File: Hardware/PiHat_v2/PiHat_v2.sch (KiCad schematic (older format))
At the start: 31 parts, among them P1 CONN_02X20, P2 CONN_01X02, P3 CONN_01X08

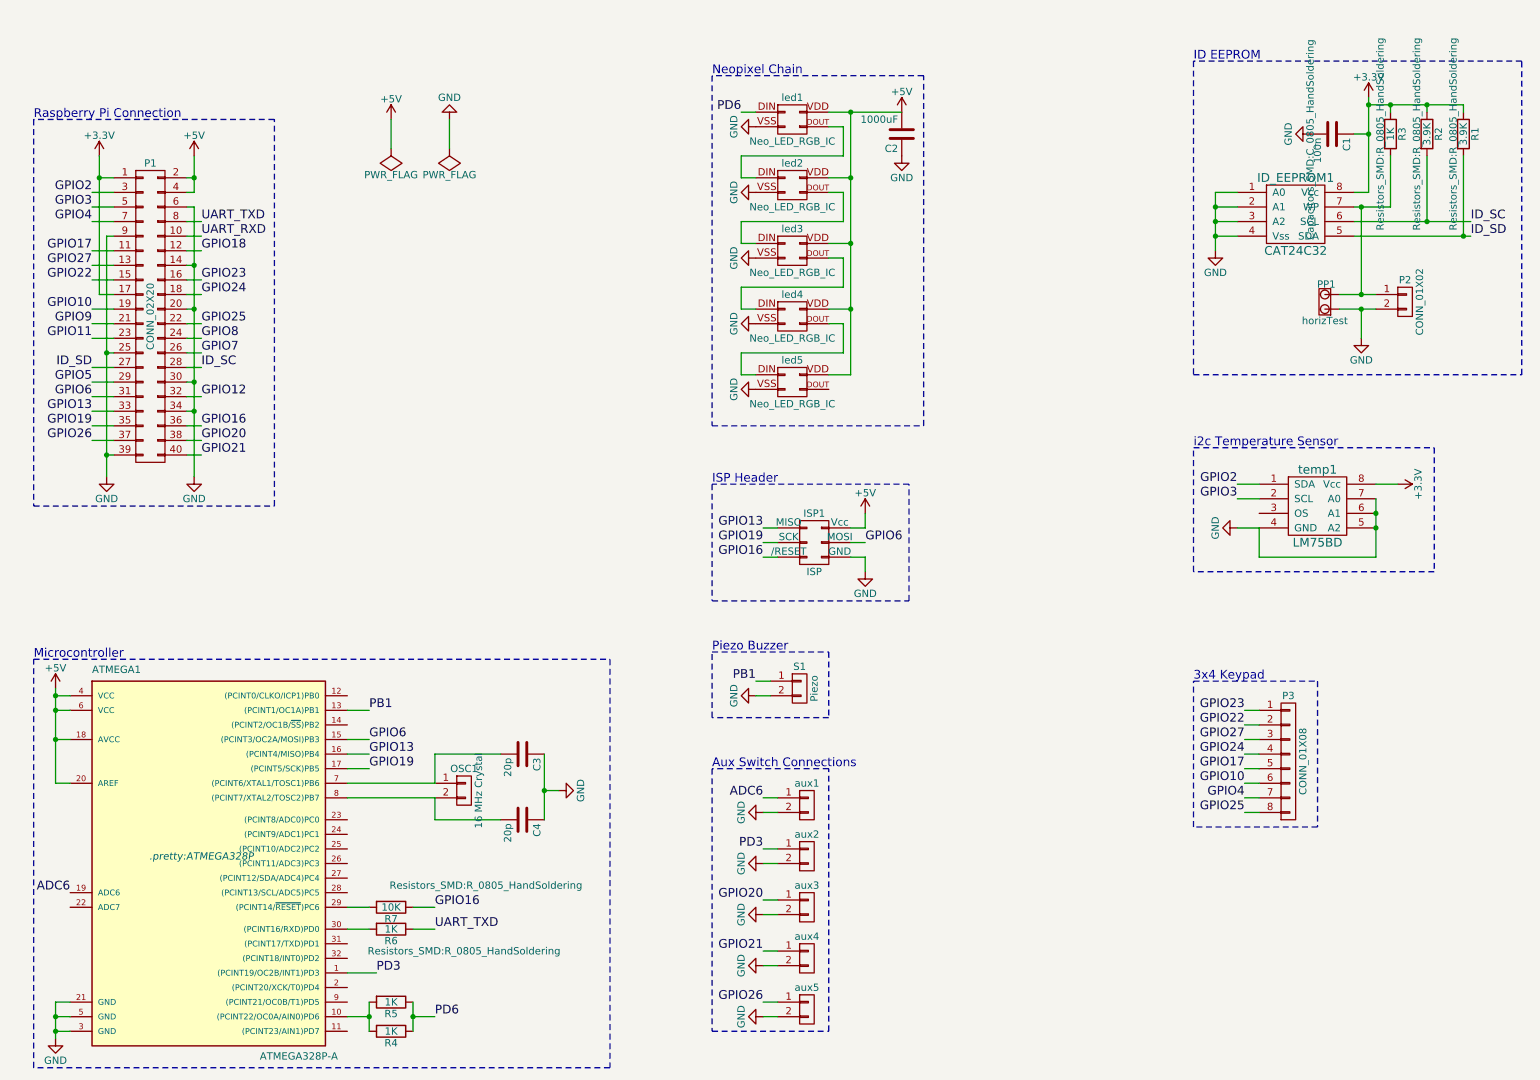
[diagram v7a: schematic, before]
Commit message: Update Aux Connector Pin Directions
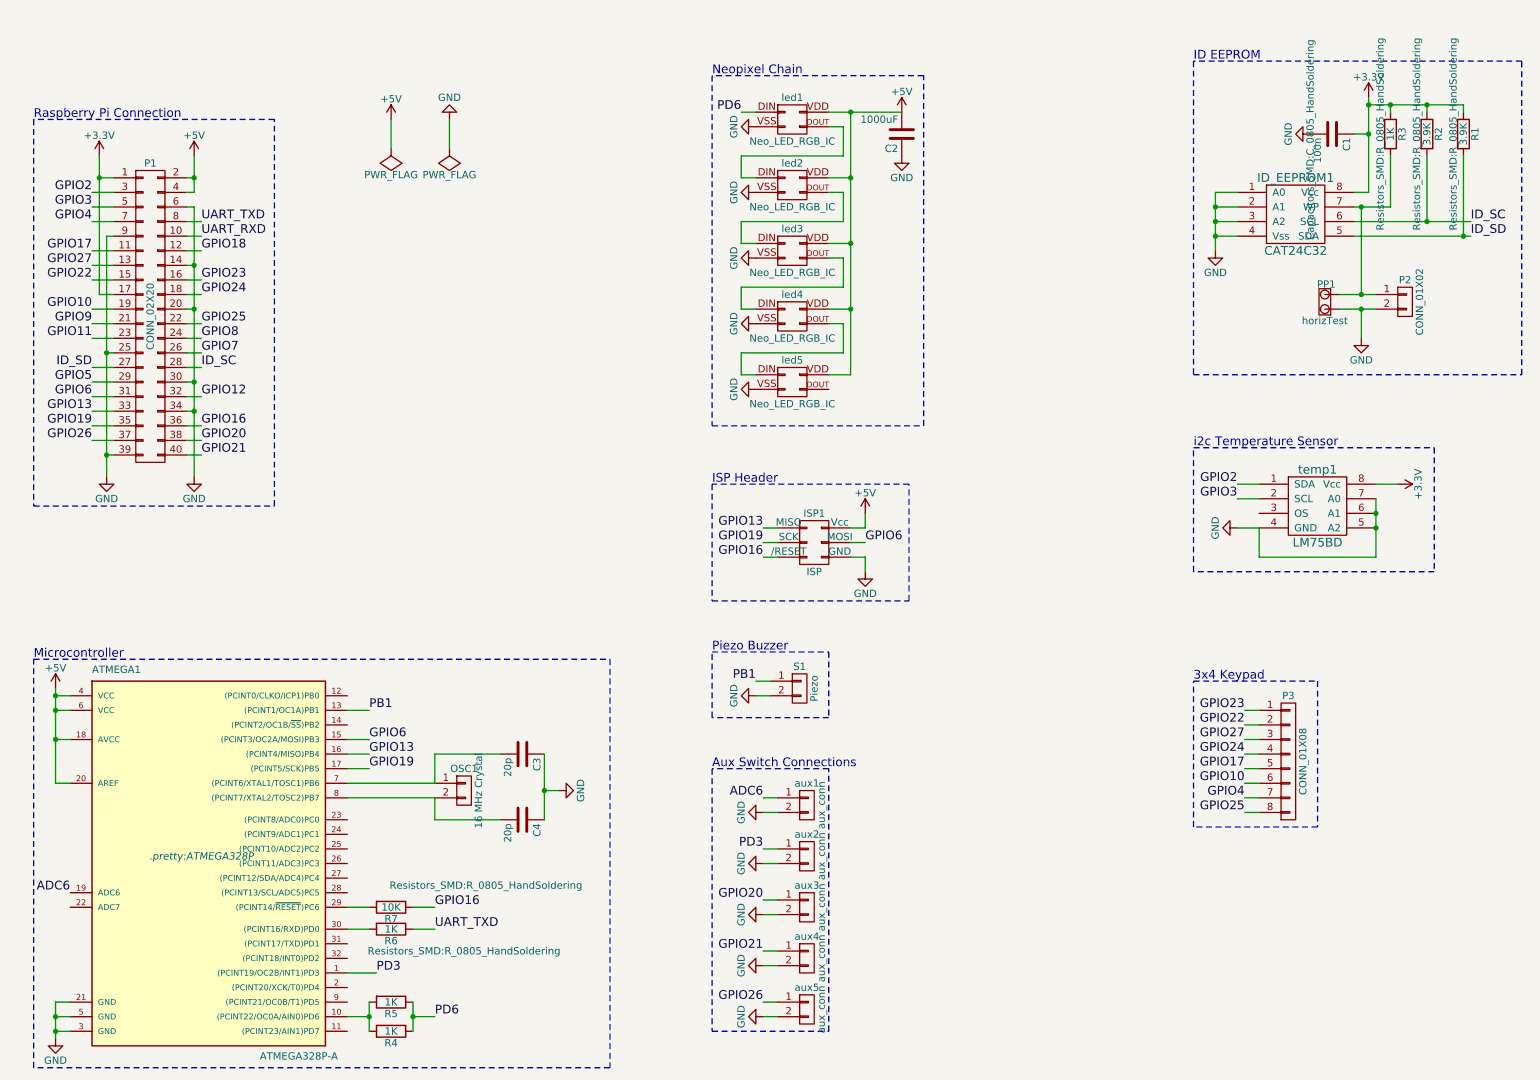
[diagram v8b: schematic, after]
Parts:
- removed aux1, aux2, aux3, aux4, aux5: CONN_01X02, Connectors_Molex:Molex_KK-6410-02_02x2.54mm_Straight, symbol CONN_01X02
- added aux1, aux2, aux3, aux4, aux5: aux_conn, symbol aux_conn
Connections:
- net ADC6: now also aux1.1 (P1)
- net GND: now also aux1.2 (P2), aux2.2 (P2), aux3.2 (P2), aux4.2 (P2), aux5.2 (P2)
- net GPIO20: now also aux3.1 (P1)
- net GPIO21: now also aux4.1 (P1)
- net GPIO26: now also aux5.1 (P1)
- net PD3: now also aux2.1 (P1)
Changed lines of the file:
@@
-$EndComp
-$Comp
-L CONN_01X02 aux1
-U 1 1 5888D1B3
-P 6050 5850
-F 0 "aux1" H 6050 6000 50  0000 C CNN
-F 1 "CONN_01X02" V 6150 5850 50  0001 C CNN
-F 2 "Connectors_Molex:Molex_KK-6410-02_02x2.54mm_Straight" H 6050 5850 50  0001 C CNN
-F 3 "" H 6050 5850 50  0000 C CNN
-	1    6050 5850
-	1    0    0    -1
 $EndComp
 $Comp
@@
 $EndComp
 $Comp
-L CONN_01X02 aux3
-U 1 1 588926FD
-P 6050 6550
-F 0 "aux3" H 6050 6700 50  0000 C CNN
-F 1 "CONN_01X02" V 6150 6550 50  0001 C CNN
-F 2 "Connectors_Molex:Molex_KK-6410-02_02x2.54mm_Straight" H 6050 6550 50  0001 C CNN
-F 3 "" H 6050 6550 50  0000 C CNN
-	1    6050 6550
-	1    0    0    -1
-$EndComp
-$Comp
 L GND #PWR011
 U 1 1 58893B93
@@
 $EndComp
 $Comp
-L CONN_01X02 aux2
-U 1 1 58893B9A
-P 6050 6200
-F 0 "aux2" H 6050 6350 50  0000 C CNN
-F 1 "CONN_01X02" V 6150 6200 50  0001 C CNN
-F 2 "Connectors_Molex:Molex_KK-6410-02_02x2.54mm_Straight" H 6050 6200 50  0001 C CNN
-F 3 "" H 6050 6200 50  0000 C CNN
-	1    6050 6200
-	1    0    0    -1
-$EndComp
-$Comp
 L GND #PWR012
 U 1 1 58893BEF
@@
 	1    5750 6950
 	0    1    1    0
-$EndComp
-$Comp
-L CONN_01X02 aux4
-U 1 1 58893BF6
-P 6050 6900
-F 0 "aux4" H 6050 7050 50  0000 C CNN
-F 1 "CONN_01X02" V 6150 6900 50  0001 C CNN
-F 2 "Connectors_Molex:Molex_KK-6410-02_02x2.54mm_Straight" H 6050 6900 50  0001 C CNN
-F 3 "" H 6050 6900 50  0000 C CNN
-	1    6050 6900
-	1    0    0    -1
 $EndComp
 $Comp
@@
 F 3 "" H 5950 -50 50  0000 C CNN
 	1    5950 1150
-	1    0    0    -1
-$EndComp
-$Comp
-L CONN_01X02 aux5
-U 1 1 58941875
-P 6050 7250
-F 0 "aux5" H 6050 7400 50  0000 C CNN
-F 1 "CONN_01X02" V 6150 7250 50  0001 C CNN
-F 2 "Connectors_Molex:Molex_KK-6410-02_02x2.54mm_Straight" H 6050 7250 50  0001 C CNN
-F 3 "" H 6050 7250 50  0000 C CNN
-	1    6050 7250
 	1    0    0    -1
 $EndComp
@@
 Connection ~ 900  5200
 Wire Wire Line
-	1000 5200 900  5200
+	900  5200 1000 5200
 Wire Notes Line
 	750  4850 4700 4850
@@
 Connection ~ 900  7400
 Wire Wire Line
-	1000 7400 900  7400
+	900  7400 1000 7400
 Wire Wire Line
 	900  7200 900  7450
@@
 Connection ~ 9950 3850
 Wire Wire Line
-	9950 4150 9950 3750
+	9950 3750 9950 4150
 Wire Notes Line
 	8700 4250 8700 3400
@@
 Connection ~ 9950 3950
 Wire Wire Line
-	9150 4150 9950 4150
-Wire Wire Line
-	9150 3950 9150 4150
+	9950 4150 9150 4150
+Wire Wire Line
+	9150 4150 9150 3950
 Wire Wire Line
 	9150 5900 9050 5900
@@
 	9950 3650 10100 3650
 Wire Wire Line
-	9000 3950 9150 3950
+	9150 3950 9000 3950
 Wire Wire Line
 	9000 3650 9150 3650
@@
 Wire Wire Line
 	3600 1150 3600 1350
+$Comp
+L aux_conn aux1
+U 1 1 5946D2A9
+P 6050 5850
+F 0 "aux1" H 6050 6000 50  0000 C CNN
+F 1 "aux_conn" V 6150 5850 50  0000 C CNN
+F 2 "" H 6050 5850 50  0000 C CNN
+F 3 "" H 6050 5850 50  0000 C CNN
+	1    6050 5850
+	1    0    0    -1
+$EndComp
+$Comp
+L aux_conn aux2
+U 1 1 5946D408
+P 6050 6200
+F 0 "aux2" H 6050 6350 50  0000 C CNN
+F 1 "aux_conn" V 6150 6200 50  0000 C CNN
+F 2 "" H 6050 6200 50  0000 C CNN
+F 3 "" H 6050 6200 50  0000 C CNN
+	1    6050 6200
+	1    0    0    -1
+$EndComp
+$Comp
+L aux_conn aux3
+U 1 1 5946D47A
+P 6050 6550
+F 0 "aux3" H 6050 6700 50  0000 C CNN
+F 1 "aux_conn" V 6150 6550 50  0000 C CNN
+F 2 "" H 6050 6550 50  0000 C CNN
+F 3 "" H 6050 6550 50  0000 C CNN
+	1    6050 6550
+	1    0    0    -1
+$EndComp
+$Comp
+L aux_conn aux4
+U 1 1 5946D4EB
+P 6050 6900
+F 0 "aux4" H 6050 7050 50  0000 C CNN
+F 1 "aux_conn" V 6150 6900 50  0000 C CNN
+F 2 "" H 6050 6900 50  0000 C CNN
+F 3 "" H 6050 6900 50  0000 C CNN
+	1    6050 6900
+	1    0    0    -1
+$EndComp
+$Comp
+L aux_conn aux5
+U 1 1 5946D55F
+P 6050 7250
+F 0 "aux5" H 6050 7400 50  0000 C CNN
+F 1 "aux_conn" V 6150 7250 50  0000 C CNN
+F 2 "" H 6050 7250 50  0000 C CNN
+F 3 "" H 6050 7250 50  0000 C CNN
+	1    6050 7250
+	1    0    0    -1
+$EndComp
 $EndSCHEMATC
